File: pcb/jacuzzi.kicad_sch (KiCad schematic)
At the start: 89 parts, among them J1 Conn_01x03, J10 Conn_01x02, J11 Conn_01x03, J12 Conn_01x03, J19 Conn_01x03, J2 Conn_01x03, J3 Conn_01x03, J4 Conn_02x02_Counter_Clockwise_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, J5 Conn_01x03, J6 Conn_01x03, J7 Conn_01x02, J8 Conn_01x06, J9 USB_C_Receptacle_PowerOnly_6P, K1 SRD-05VDC, Q1 MMBT3904, Q2 MMBT3904, Q3 MMBT3904, Q4 IRF4905STRLPBF, Q5 MMBT3904, Q6 IRF4905STRLPBF, Q7 MMBT3904, U1 LM2575-3.3BU, U2 LM2575-5.0BU, U3 ESP32-DEVKITC-32U, U4 DM-OLED096-636

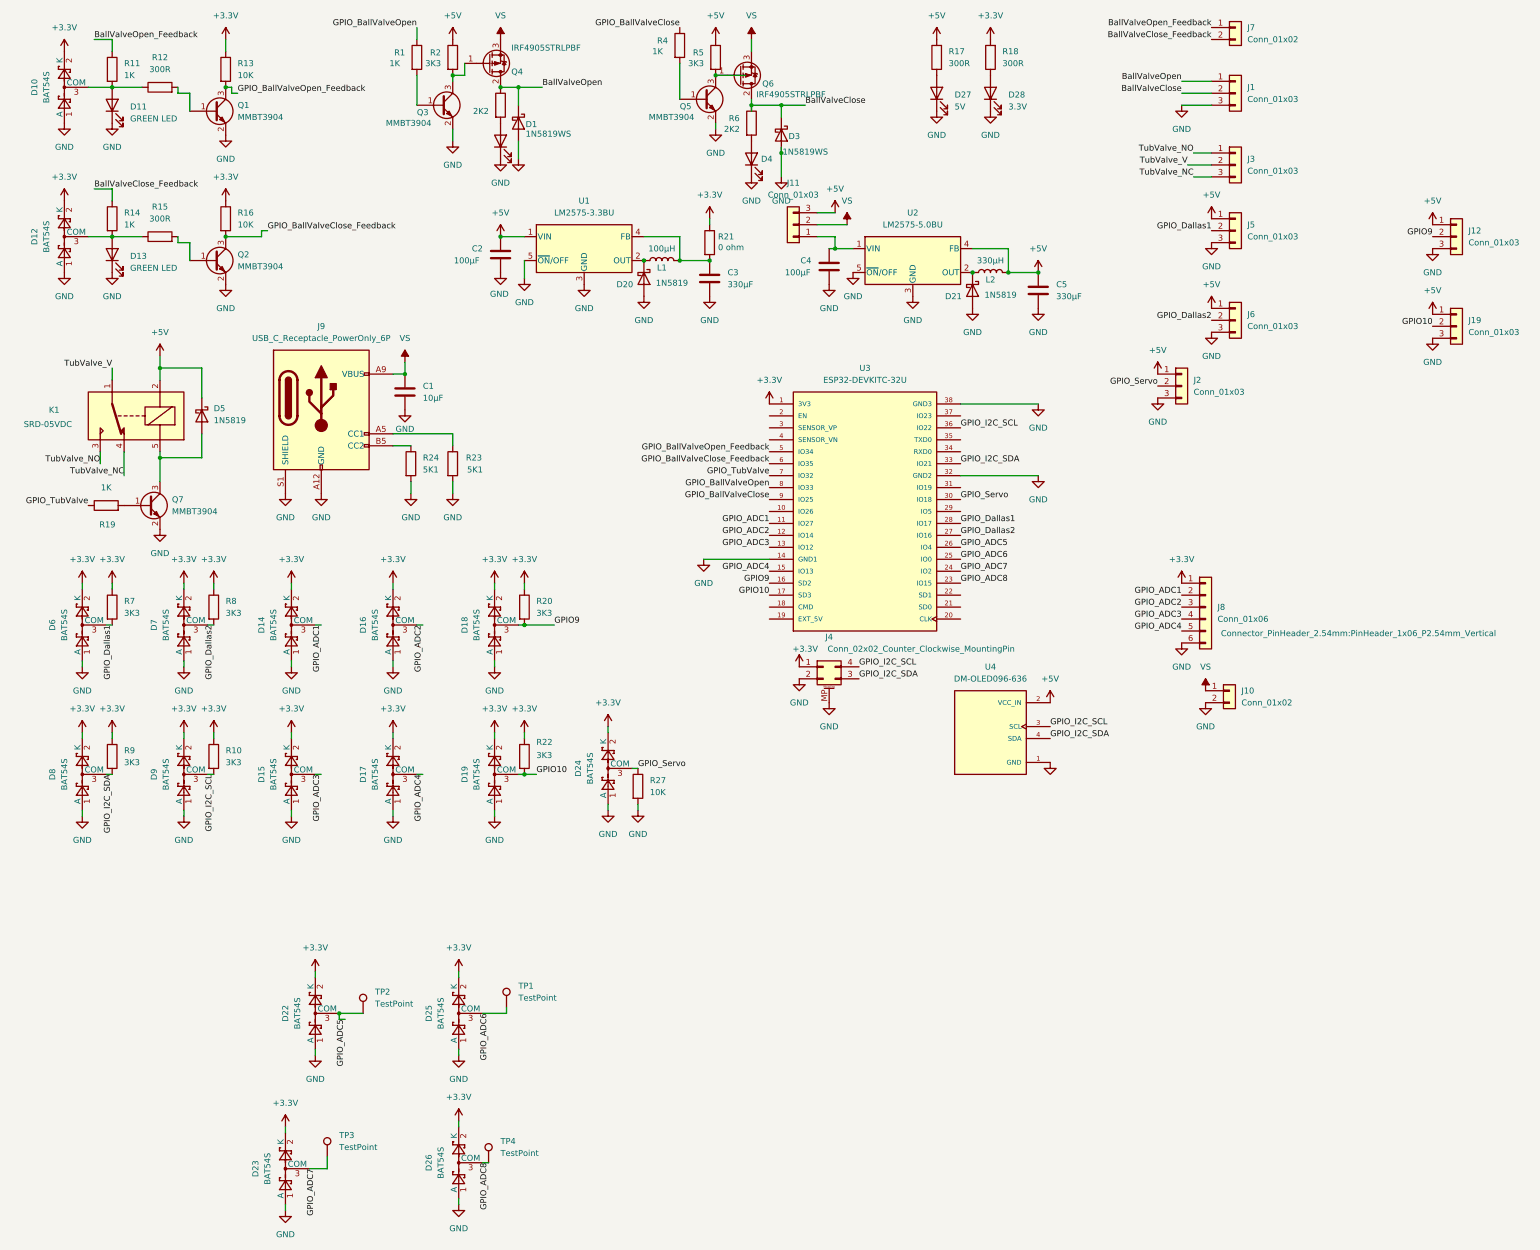
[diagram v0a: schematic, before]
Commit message: added k2 and chagend the output fet ready for rewive
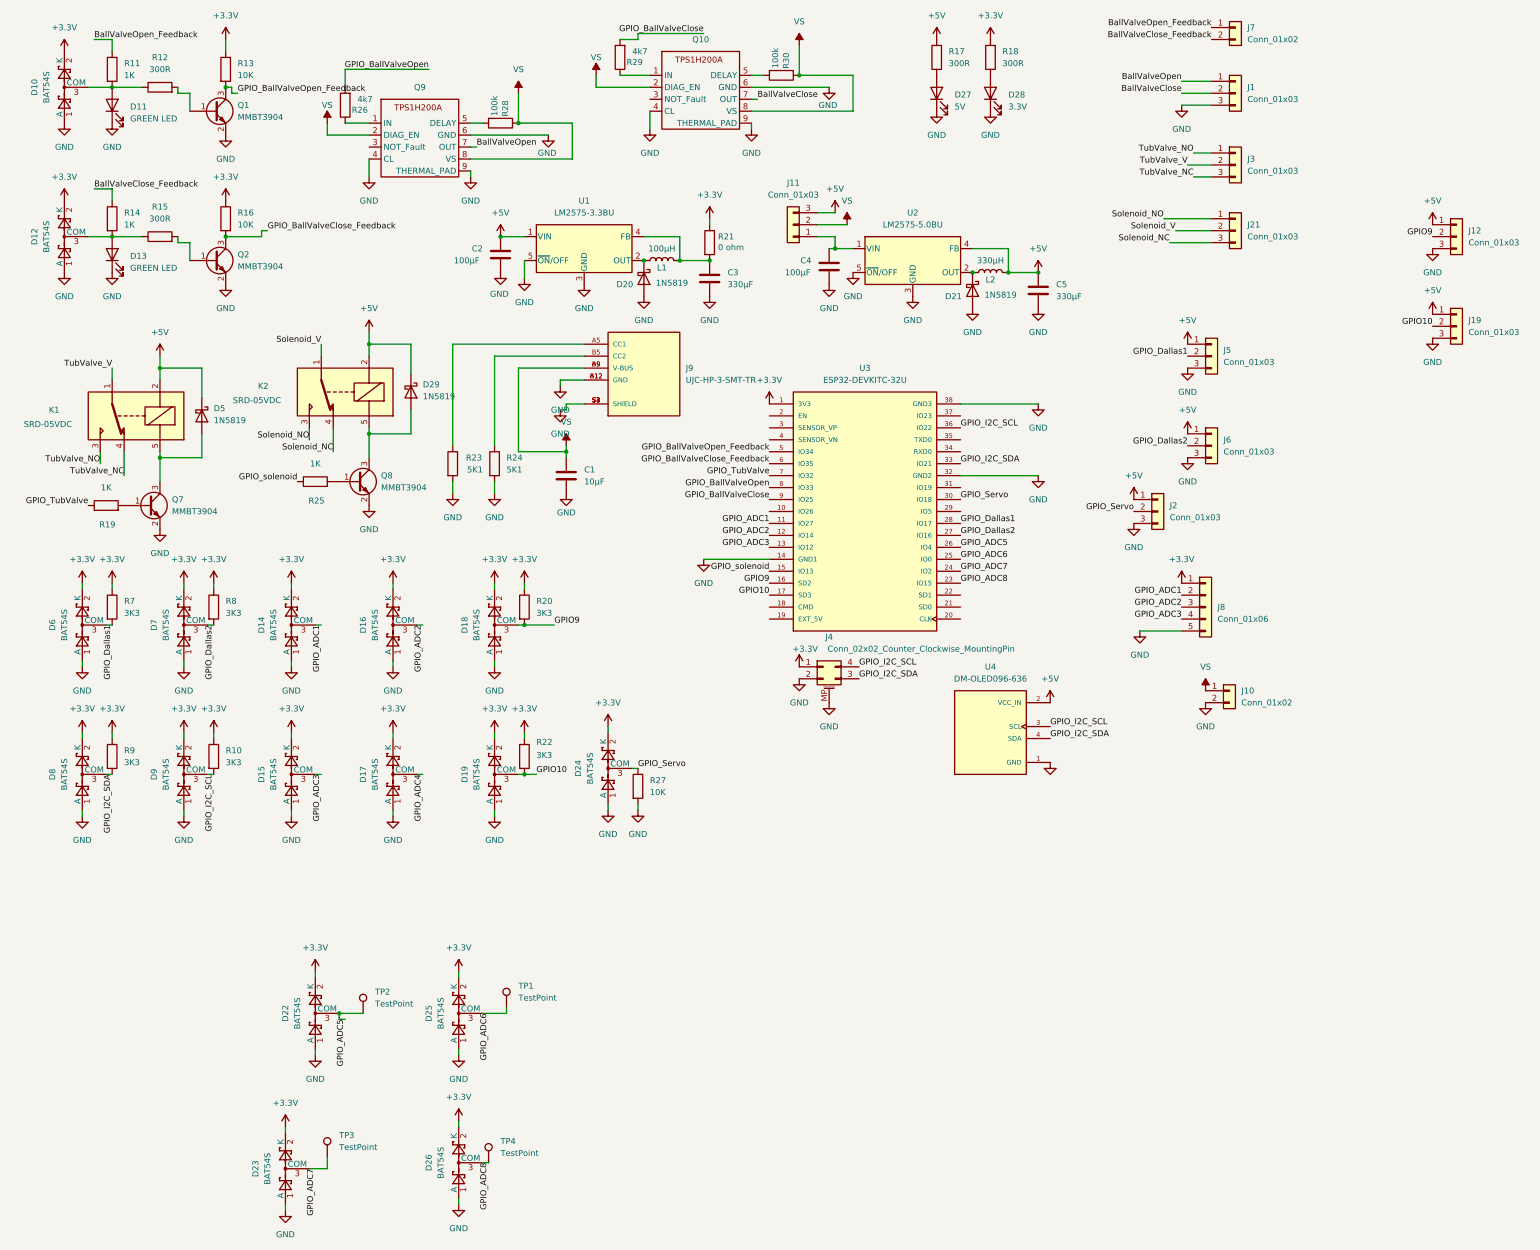
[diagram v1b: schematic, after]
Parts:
- removed D1, D3: 1N5819WS, Diode_SMD:D_SOD-323, symbol Diode:1N5819WS
- removed D2, D4: GREEN LED, LED_SMD:LED_0805_2012Metric, symbol Device:LED
- removed J9: USB_C_Receptacle_PowerOnly_6P, Connector_USB:USB_C_Receptacle_GCT_USB4135-GF-A_6P_TopMnt_Horizontal, symbol Connector:USB_C_Receptacle_PowerOnly_6P
- removed Q3, Q5: MMBT3904, Package_TO_SOT_SMD:SOT-23, symbol Transistor_BJT:MMBT3904
- removed Q4, Q6: IRF4905STRLPBF, Package_TO_SOT_SMD:TO-263-2, symbol Transistor_FET:IRF4905
- removed R1, R4: 1K, Resistor_SMD:R_0805_2012Metric, symbol Device:R
- removed R2, R5: 3K3, Resistor_SMD:R_0805_2012Metric, symbol Device:R
- removed R3, R6: 2K2, Resistor_SMD:R_0805_2012Metric, symbol Device:R
- added D29: 1N5819, Diode_SMD:D_SOD-323, symbol Device:D_Schottky
- added J21: Conn_01x03, Connector_Phoenix_MC_HighVoltage:PhoenixContact_MCV_1,5_3-G-5.08_1x03_P5.08mm_Vertical, symbol Connector_Generic:Conn_01x03
- added J9: UJC-HP-3-SMT-TR, UJC-HP-3-SMT-TR:CUI_UJC-HP-3-SMT-TR, symbol UJC-HP-3-SMT-TR:UJC-HP-3-SMT-TR
- added K2: SRD-05VDC, Relay_THT:Relay_SPDT_SANYOU_SRD_Series_Form_C, symbol Relay:G5LE-1
- added Q10, Q9: ~, Package_SO:HVSSOP-8-1EP_3x3mm_P0.65mm_EP1.57x1.89mm, symbol custom:TPS1H200A
- added Q8: MMBT3904, Package_TO_SOT_SMD:SOT-23, symbol Transistor_BJT:MMBT3904
- added R25: 1K, Resistor_SMD:R_0805_2012Metric, symbol Device:R
- added R26, R29: 4k7, Resistor_SMD:R_0805_2012Metric, symbol Device:R
- added R28, R30: 100k, Resistor_SMD:R_0805_2012Metric, symbol Device:R
- J8: footprint Connector_PinHeader_2.54mm:PinHeader_1x06_P2.54mm_Vertical -> Connector_PinHeader_2.54mm:PinHeader_1x05_P2.54mm_Vertical; symbol Connector_Generic:Conn_01x06 -> Connector_Generic:Conn_01x05
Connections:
- net +5V: now also D29.1 (K), K2.2
- net BallValveClose: now also Q10.7 (OUT)
- net BallValveOpen: now also Q9.7 (OUT)
- net GND: now also J8.5 (Pin_5), J9.A12 (GND), J9.B12 (GND), J9.S1 (SHIELD), J9.S2 (SHIELD), J9.S3 (SHIELD), J9.S4 (SHIELD), Q10.4 (CL), Q10.6 (GND), Q10.9 (THERMAL_PAD), Q8.2 (E), Q9.4 (CL), Q9.6 (GND), Q9.9 (THERMAL_PAD); no longer J8.6 (Pin_6)
- net GPIO_ADC4: no longer J8.5 (Pin_5), U3.15 (IO13)
- net GPIO_BallValveClose: now also R29.2
- net GPIO_BallValveOpen: now also R26.2
- net VS: now also J9.A9 (V-BUS), J9.B9 (V-BUS), Q10.2 (DIAG_EN), Q10.8 (VS), Q9.2 (DIAG_EN), Q9.8 (VS), R28.1, R30.1
- net at R23.1: now also J9.A5 (CC1)
- net at R24.1: now also J9.B5 (CC2)
- new net: Q9.5 (DELAY), R28.2
- new net: Q9.1 (IN), R26.1
- new net: Q8.1 (B), R25.2
- new net: Q10.1 (IN), R29.1
- new net: D29.2 (A), K2.5, Q8.3 (C)
- new net: Q10.5 (DELAY), R30.2
- new net GPIO_solenoid: R25.1, U3.15 (IO13)
- new net Solenoid_NC: J21.3 (Pin_3), K2.4
- new net Solenoid_NO: J21.1 (Pin_1), K2.3
- new net Solenoid_V: J21.2 (Pin_2), K2.1
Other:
- moved on the sheet: C1, J2, J5, J6, R24

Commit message: fixed part list
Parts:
- added R1: 0R, Resistor_SMD:R_0805_2012Metric, symbol Device:R
- J11: footprint Connector_PinHeader_2.54mm:PinHeader_1x03_P2.54mm_Vertical_SMD_Pin1Left -> Connector_PinHeader_2.54mm:PinHeader_1x03_P2.54mm_Vertical
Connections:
- net GND: now also J10.1 (Pin_1); no longer J10.2 (Pin_2)
- net VS: now also J10.2 (Pin_2), R1.2; no longer J10.1 (Pin_1), Q10.2 (DIAG_EN), Q10.8 (VS), Q9.2 (DIAG_EN), Q9.8 (VS)
- new net VS 5mills: Q10.2 (DIAG_EN), Q10.8 (VS), Q9.2 (DIAG_EN), Q9.8 (VS), R1.1
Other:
- moved on the sheet: J10, R28

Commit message: minor fixes and ordered
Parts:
- J9: LCSC (none) -> C668623
- Q10, Q9: LCSC (none) -> C2653785
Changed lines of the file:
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@@
 			)
 		)
+		(property "LCSC" "C2653785"
+			(at 97.155 29.21 0)
+			(effects
+				(font
+					(size 1.27 1.27)
+				)
+				(hide yes)
+			)
+		)
 		(pin "1"
 		)
@@
 			)
 		)
+		(property "LCSC" "C668623"
+			(at 153.67 88.8999 0)
+			(effects
+				(font
+					(size 1.27 1.27)
+				)
+				(hide yes)
+			)
+		)
 		(pin "S2"
 		)
@@
 			(effects
 				(font
+					(size 1.27 1.27)
+				)
+				(hide yes)
+			)
+		)
+		(property "LCSC" "C2653785"
+			(at 156.845 19.05 0)
+			(effects
+				(font

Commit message: old changes dont know what they are
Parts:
- R1: LCSC C17617 -> C17477
- R26, R29: LCSC C26010 -> C17673
- R28, R30: LCSC C26010 -> C149504
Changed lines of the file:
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@@
 			)
 		)
-		(property "LCSC" "C26010"
+		(property "LCSC" "C149504"
 			(at 119.126 32.004 0)
 			(effects
@@
 			)
 		)
-		(property "LCSC" "C17617"
+		(property "LCSC" "C17477"
 			(at 115.5699 24.13 0)
 			(effects
@@
 			)
 		)
-		(property "LCSC" "C26010"
+		(property "LCSC" "C17673"
 			(at 144.526 23.876 0)
 			(effects
@@
 			)
 		)
-		(property "LCSC" "C26010"
+		(property "LCSC" "C149504"
 			(at 175.006 21.844 0)
 			(effects
@@
 			)
 		)
-		(property "LCSC" "C26010"
+		(property "LCSC" "C17673"
 			(at 86.106 34.036 0)
 			(effects
